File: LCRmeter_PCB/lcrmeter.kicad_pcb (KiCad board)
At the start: 2 copper layers, 71.9 x 54.1 mm, 63 parts, among them J1 LCR_input, J2 LCR_input, J3 Conn_01x06, J4 USB_B_Micro, J5 OSCILLOSCOPE, J6 misc, J7 misc, SW1 power, SW2 +, SW3 -, SW4 ok, SW5 back, U1 MCP47, U2 STM32F103C8Tx, U3 OLED, U4 74HC14, U5 MCP6001-OT, Y1 8Mhz

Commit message: added brief documentation for part of software, and license
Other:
- board text added: "COPYRIGHT(c) 2019 Rafał Mazurkiewicz"
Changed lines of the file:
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@@
   (general
     (thickness 1.6)
-    (drawings 8)
+    (drawings 9)
     (tracks 919)
     (zones 0)
@@
     )
   )
+  (gr_text "COPYRIGHT(c) 2019 Rafał Mazurkiewicz" (at 152.55 146.5) (layer B.SilkS)
+    (effects (font (size 1.5 1.5) (thickness 0.3)) (justify mirror))
+  )
   (dimension 54.102 (width 0.3) (layer Cmts.User)

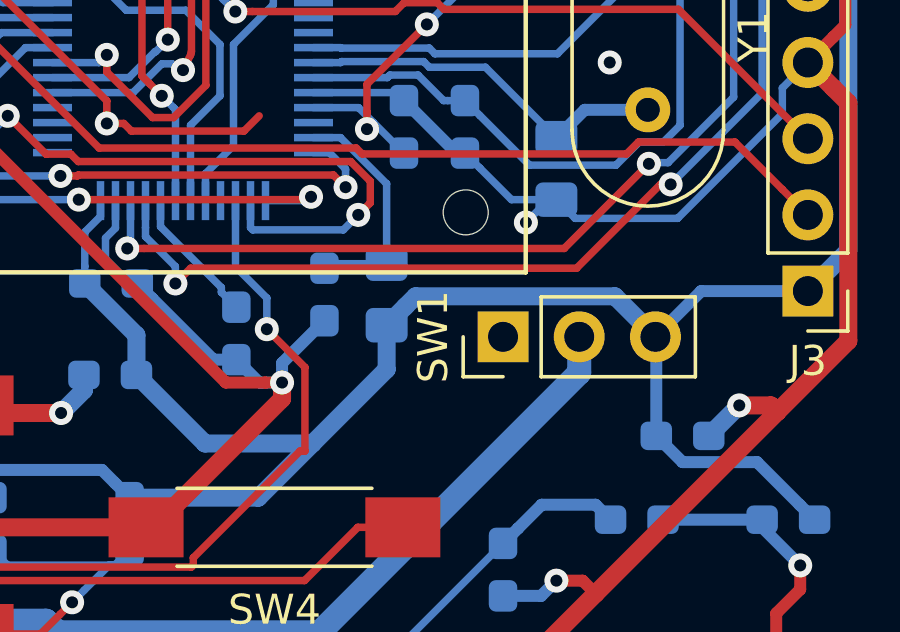
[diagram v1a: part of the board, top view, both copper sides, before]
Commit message: fixed schematic- diode reference and minor problems
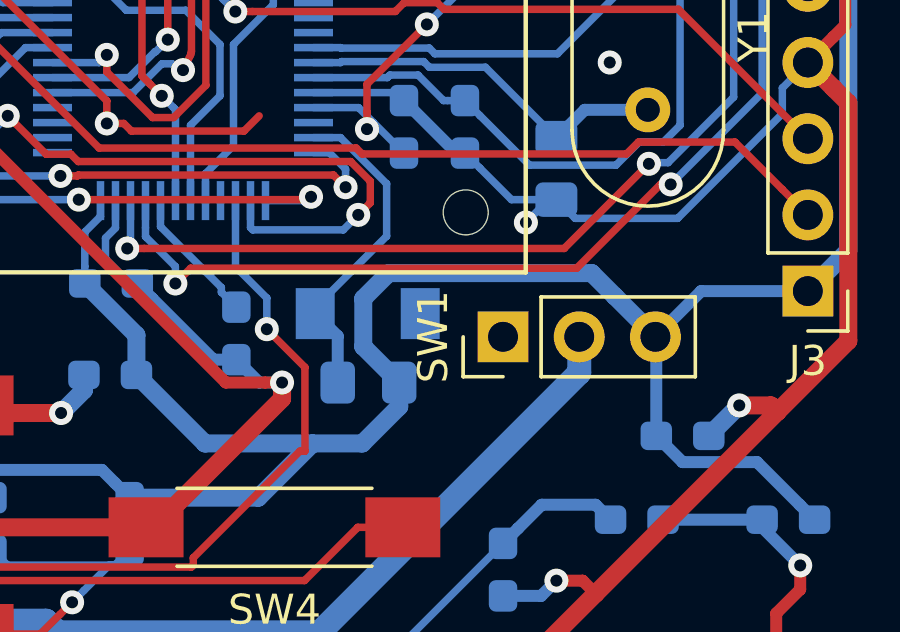
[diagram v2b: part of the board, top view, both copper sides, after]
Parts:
- removed R20: 10k, Resistor_SMD:R_0603_1608Metric_Pad1.05x0.95mm_HandSolder
- added D1: 2V, Diode_SMD:D_MiniMELF, B.Cu at (158.1, 134.1)
- J3: value Conn_01x06 -> Prog_interface
- moved R19 3.00 mm to (158.1, 136.4), turned to 180 degrees
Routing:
- net VCC: track 276.7 -> 280.3 mm
- net Net-(D1-Pad1): track 7.88 -> 11.0 mm
- net GND: track 409.3 -> 406.7 mm

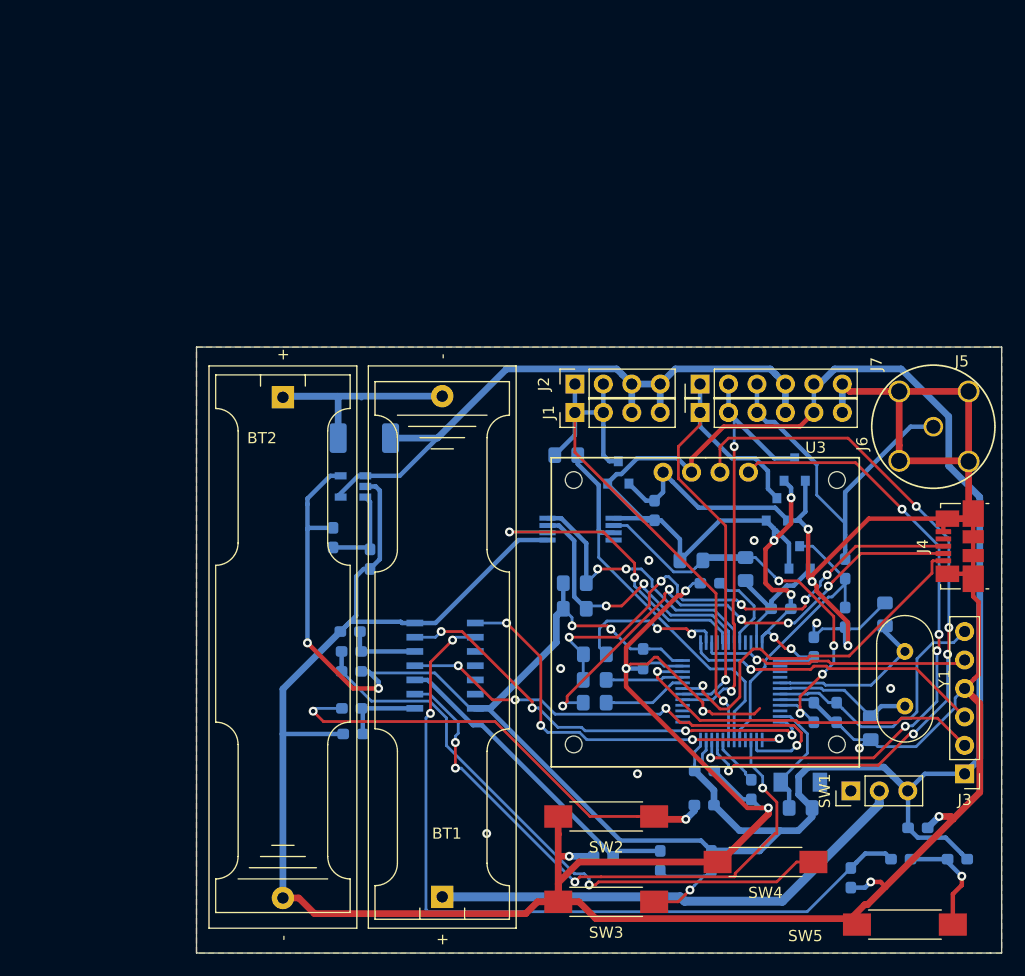
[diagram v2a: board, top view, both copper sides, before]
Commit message: placed components on PCB
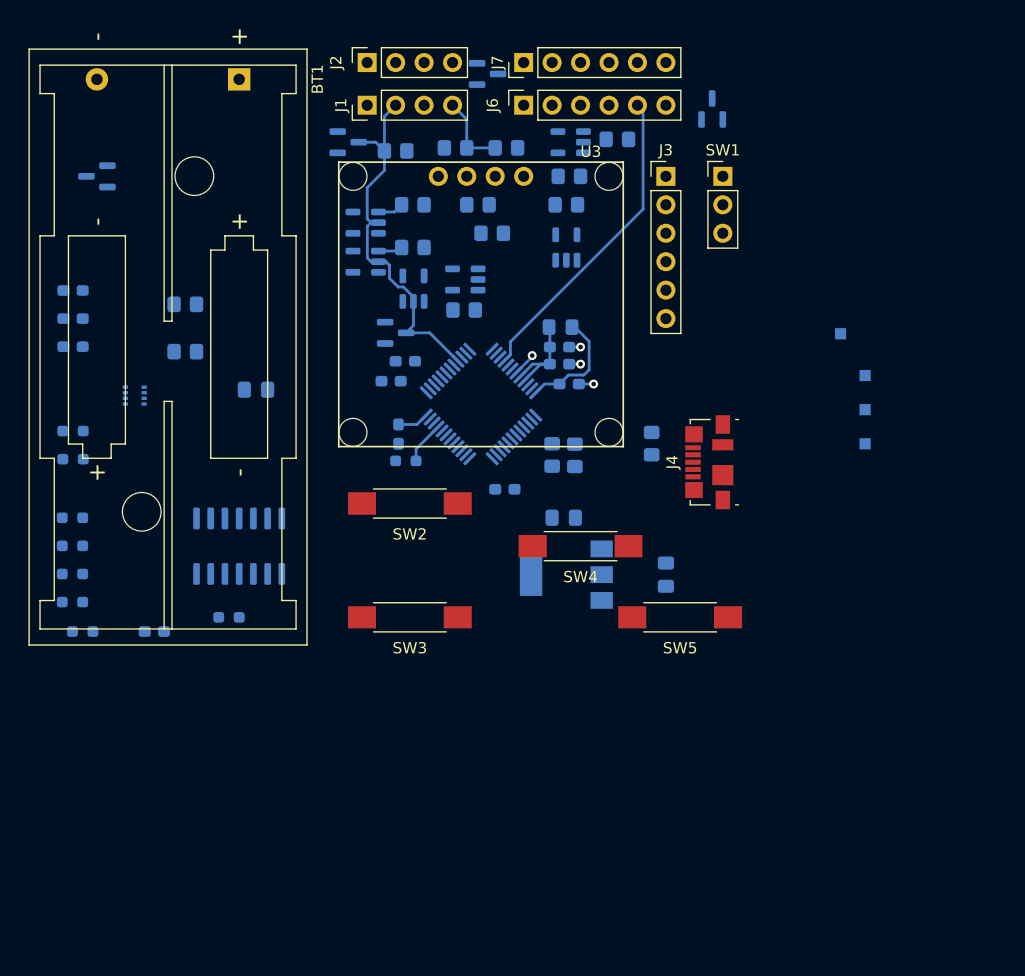
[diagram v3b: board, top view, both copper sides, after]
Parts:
- removed BT2: Batt, Battery:BatteryHolder_Keystone_2466_1xAAA
- removed C1, C2: 20pF, Capacitor_SMD:C_0805_2012Metric_Pad1.15x1.40mm_HandSolder
- removed C6: 100n, Capacitor_SMD:C_0603_1608Metric_Pad1.05x0.95mm_HandSolder
- removed D1: 2V, Diode_SMD:D_MiniMELF
- removed D5: BAT54S, Package_TO_SOT_SMD:SOT-23
- removed J5: OSCILLOSCOPE, footprints:BNC TE CONNECTIVITY 5-1634503
- removed Y1: 8Mhz, Crystal:Crystal_HC49-U_Vertical
- added C18: 10u, Capacitor_SMD:C_0805_2012Metric_Pad1.18x1.45mm_HandSolder, B.Cu at (146.1, 115.6)
- added C19: 10u, Capacitor_SMD:C_0805_2012Metric_Pad1.18x1.45mm_HandSolder, B.Cu at (136.9, 110.5)
- added D6: BAT54CW, Package_TO_SOT_SMD:SOT-23, B.Cu at (95.2, 80.0)
- added IC1: TPS2116DRLR, Library_Loader:SOTFL50P160X60-8N, B.Cu at (98.6, 99.6)
- added Q1: NX7002BKR, Package_TO_SOT_SMD:SOT-23, B.Cu at (121.9, 94.0)
- added R20: 0, Resistor_SMD:R_0805_2012Metric_Pad1.20x1.40mm_HandSolder, B.Cu at (128.0, 91.9)
- added R24: 1k5, Resistor_SMD:R_0805_2012Metric_Pad1.20x1.40mm_HandSolder, B.Cu at (103.1, 91.4)
- added R25: 2k2, Resistor_SMD:R_0805_2012Metric_Pad1.20x1.40mm_HandSolder, B.Cu at (103.1, 95.7)
- added TP1: TestPoint, TestPoint:TestPoint_Pad_1.0x1.0mm, B.Cu at (161.6, 94.1)
- added TP2: TestPoint, TestPoint:TestPoint_Pad_1.0x1.0mm, B.Cu at (163.8, 97.8)
- added TP3: TestPoint, TestPoint:TestPoint_Pad_1.0x1.0mm, B.Cu at (163.8, 100.8)
- added TP4: TestPoint, TestPoint:TestPoint_Pad_1.0x1.0mm, B.Cu at (163.8, 103.9)
- added U10: MCP6001-OT, Package_TO_SOT_SMD:SOT-23-5, B.Cu at (137.2, 86.4)
- added U6: STM32G473C_B-C-E_Tx, Package_QFP:LQFP-48_7x7mm_P0.5mm, B.Cu at (129.5, 100.3)
- added U7: 74LVC1G66, Package_TO_SOT_SMD:SOT-23-5, B.Cu at (123.5, 90.0)
- added U8: MCP6001-OT, Package_TO_SOT_SMD:SOT-23-5, B.Cu at (137.5, 77.0)
- added U9: LM1117MP-3.3, Package_TO_SOT_SMD:SOT-223-3_TabPin2, B.Cu at (137.2, 115.6)
- BT1: footprint Battery:BatteryHolder_Keystone_2466_1xAAA -> Battery:BatteryHolder_Keystone_2468_2xAAA
- C10, C12, C13, C14, C15, C3, C4, C5, C7, C9: footprint Capacitor_SMD:C_0603_1608Metric_Pad1.05x0.95mm_HandSolder -> Capacitor_SMD:C_0603_1608Metric_Pad1.08x0.95mm_HandSolder
- C11: footprint Capacitor_SMD:C_0805_2012Metric_Pad1.15x1.40mm_HandSolder -> Capacitor_SMD:C_0603_1608Metric_Pad1.08x0.95mm_HandSolder
- C8: footprint Capacitor_SMD:C_0603_1608Metric_Pad1.05x0.95mm_HandSolder -> Capacitor_SMD:C_0805_2012Metric_Pad1.18x1.45mm_HandSolder
- R1, R15: footprint Resistor_SMD:R_0805_2012Metric_Pad1.15x1.40mm_HandSolder -> Resistor_SMD:R_0805_2012Metric_Pad1.20x1.40mm_HandSolder
- R10, R11, R12, R13, R2, R4, R5, R6, R9: footprint Resistor_SMD:R_0603_1608Metric_Pad1.05x0.95mm_HandSolder -> Resistor_SMD:R_0603_1608Metric_Pad0.98x0.95mm_HandSolder
- R14, R16: value 22 -> 1k5; footprint Resistor_SMD:R_0805_2012Metric_Pad1.15x1.40mm_HandSolder -> Resistor_SMD:R_0805_2012Metric_Pad1.20x1.40mm_HandSolder
- R17, R3: value 10k -> 0; footprint Resistor_SMD:R_0603_1608Metric_Pad1.05x0.95mm_HandSolder -> Resistor_SMD:R_0805_2012Metric_Pad1.20x1.40mm_HandSolder
- R18: value 10k -> 2k; footprint Resistor_SMD:R_0603_1608Metric_Pad1.05x0.95mm_HandSolder -> Resistor_SMD:R_0805_2012Metric_Pad1.20x1.40mm_HandSolder
- R19: value 20k -> 500; footprint Resistor_SMD:R_0805_2012Metric_Pad1.15x1.40mm_HandSolder -> Resistor_SMD:R_0805_2012Metric_Pad1.20x1.40mm_HandSolder
- R21: footprint Resistor_SMD:R_2010_5025Metric_Pad1.52x2.65mm_HandSolder -> Resistor_SMD:R_0805_2012Metric_Pad1.20x1.40mm_HandSolder
- R22, R23: footprint Resistor_SMD:R_0603_1608Metric_Pad1.05x0.95mm_HandSolder -> Resistor_SMD:R_0805_2012Metric_Pad1.20x1.40mm_HandSolder
- R7, R8: value 3k3 -> 0; footprint Resistor_SMD:R_0805_2012Metric_Pad1.15x1.40mm_HandSolder -> Resistor_SMD:R_0805_2012Metric_Pad1.20x1.40mm_HandSolder
- SW2: value + -> up
- SW3: value - -> down
- U1: value MCP47 -> 74LVC1G66; footprint Package_SO:TSSOP-8_4.4x3mm_P0.65mm -> Package_TO_SOT_SMD:SOT-23-5
- U2: value STM32F103C8Tx -> 74LVC1G66; footprint Package_QFP:LQFP-48_7x7mm_P0.5mm -> Package_TO_SOT_SMD:SOT-23-5
- moved C13 87.0 mm to (93.1, 90.2), turned to 180 degrees
- moved R5 86.7 mm to (93.1, 105.3)
- moved R11 79.1 mm to (93.1, 113.0), turned to 180 degrees
- moved BT1 75.2 mm to (108.0, 71.3), turned to -90 degrees
- moved C8 70.9 mm to (109.5, 99.1), turned to 180 degrees
- moved C15 65.7 mm to (93.1, 95.2)
- moved R19 64.0 mm to (123.5, 82.5)
- moved R9 59.7 mm to (94.0, 120.7), turned to 180 degrees
- moved J3 59.6 mm to (146.1, 80.0), turned to 0 degrees
- moved R13 57.3 mm to (93.1, 118.0), turned to 180 degrees
- moved SW1 56.0 mm to (151.1, 80.0), turned to 0 degrees
- moved R17 51.2 mm to (127.3, 77.5), turned to 180 degrees
- moved R18 50.8 mm to (123.5, 86.4), turned to 180 degrees
- moved U2 50.4 mm to (119.2, 87.6)
- moved C10 49.7 mm to (122.8, 96.5), turned to 0 degrees
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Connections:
- BT1 pad 2: Net-(BT1-Pad2) -> GND
- D3 pad 3: /OSCILLOSCOPE -> /OSCILLOSCOPE_IN
- J1 pad 3: +1V5 -> Net-(J1-Pin_3)
- J1 pad 4: +1V5 -> Net-(J1-Pin_3)
- J2 pad 3: +1V5 -> Net-(J1-Pin_3)
- J2 pad 4: +1V5 -> Net-(J1-Pin_3)
- J3 pad 2: Net-(J3-Pad2) -> Net-(J3-Pin_2)
- J3 pad 3: Net-(J3-Pad3) -> Net-(J3-Pin_3)
- J4 pad 1: /VBUS -> VBUS
- J4 pad 2: Net-(J4-Pad2) -> /USB_-
- J4 pad 3: Net-(J4-Pad3) -> /USB_+
- J4 pad 4: Net-(J4-Pad4) -> unconnected-(J4-ID-Pad4)
- J4 pad 6: GND -> unconnected-(J4-Shield-Pad6)
- J6 pad 1: /PWM_OUT -> VCC
- J6 pad 2: /8_MHz_OUT -> /PWM_OUT
- J6 pad 3: /OSCILLOSCOPE_IN -> /WAVE_OUT
- J6 pad 4: +1V5 -> GND
- J6 pad 5: VCC -> /OSCILLOSCOPE_IN
- J7 pad 1: /PWM_OUT -> VCC
- J7 pad 2: /8_MHz_OUT -> /PWM_OUT
- J7 pad 3: /OSCILLOSCOPE_IN -> /WAVE_OUT
- J7 pad 4: +1V5 -> GND
- J7 pad 5: VCC -> /OSCILLOSCOPE_IN
- R14 pad 1: Net-(J4-Pad2) -> VCC
- R14 pad 2: /USB_- -> /SDA
- R15 pad 2: Net-(J4-Pad3) -> /USB_+
- R16 pad 1: Net-(J4-Pad3) -> VCC
- R16 pad 2: /USB_+ -> /SCL
- R17 pad 1: /OSCILLOSCOPE_IN -> Net-(J1-Pin_3)
- R17 pad 2: /OSCILLOSCOPE -> GND
- R18 pad 1: /OSCILLOSCOPE -> /ADC_1
- R18 pad 2: GND -> Net-(R18-Pad2)
- R19 pad 1: VCC -> /ADC_1
- R19 pad 2: Net-(D1-Pad1) -> Net-(R19-Pad2)
- R2 pad 2: Net-(R2-Pad2) -> Net-(U6-PB8)
- R21 pad 1: +1V5 -> Net-(U8-+)
- R21 pad 2: Net-(BT1-Pad2) -> +1V5
- R22 pad 1: VCC -> Net-(U8-+)
- R22 pad 2: Net-(R22-Pad2) -> VCC
- R23 pad 1: Net-(R22-Pad2) -> GND
- R23 pad 2: GND -> Net-(U8-+)
- R3 pad 1: GND -> /ADC_1
- R3 pad 2: Net-(R3-Pad2) -> /ADC_1b
- R7 pad 1: VCC -> /ADC_2
- R7 pad 2: /I2C_SCL -> /ADC_2b
- R8 pad 1: VCC -> Net-(J1-Pin_3)
- R8 pad 2: /I2C_SDA -> +1V5
- SW1 pad 1: Net-(SW1-Pad1) -> unconnected-(SW1-Pad1)
- SW1 pad 3: VCC -> +BATT
- U1 pad 1: VCC -> Net-(R19-Pad2)
- U1 pad 2: VDDA -> /ADC_2
- U1 pad 3: /ADC_1 -> GND
- U1 pad 4: Net-(U1-Pad4) -> /EN_PATH_1
- U1 pad 5: GND -> VCC
- U2 pad 1: VCC -> Net-(R18-Pad2)
- U2 pad 2: Net-(U2-Pad2) -> /ADC_2
- U2 pad 3: Net-(U2-Pad3) -> GND
- U2 pad 4: Net-(U2-Pad4) -> /EN_PATH_2
- U2 pad 5: Net-(C2-Pad1) -> VCC
- U3 pad 1: Net-(U2-Pad22) -> /SDA
- U3 pad 2: Net-(U2-Pad21) -> /SCL
- U5 pad 1: +1V5 -> /ADC_1
- U5 pad 3: Net-(R22-Pad2) -> /DAC_UNBUFFERED
- U5 pad 4: +1V5 -> /ADC_1
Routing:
- net GND: track 406.7 -> 5.51 mm, vias 18 -> 4
- net VCC: track 280.3 -> 13.0 mm, vias 9 -> 0
- net Net-(C13-Pad1): track 71.1 -> 0.00 mm, vias 2 -> 0
- net +1V5: track 67.0 -> 0.00 mm
- net Net-(U2-Pad21): track 66.5 -> 0.00 mm, vias 5 -> 0
- net Net-(U2-Pad22): track 58.3 -> 0.00 mm, vias 5 -> 0
- net Net-(R10-Pad2): track 54.4 -> 0.00 mm, vias 1 -> 0
- net /BUTTON_+: track 53.2 -> 0.00 mm, vias 4 -> 0
- net Net-(J4-Pad3): track 45.2 -> 0.00 mm, vias 5 -> 0
- net /PWM_OUT: track 45.0 -> 0.00 mm, vias 1 -> 0
- net Net-(J4-Pad2): track 45.0 -> 0.00 mm, vias 5 -> 0
- net Net-(BT1-+): track 44.0 -> 0.00 mm
- net /BUTTON_-: track 43.4 -> 0.00 mm, vias 4 -> 0
- net Net-(R12-Pad2): track 41.5 -> 0.00 mm, vias 2 -> 0
- net /8_MHz_OUT: track 40.2 -> 0.00 mm, vias 2 -> 0
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- removed copper zone on B.Cu, net GND
- removed copper zone on F.Cu, net GND
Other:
- board outline removed
- net class Default removed
- board text removed: "COPYRIGHT(c) 2019 Rafał Mazurkiewicz"

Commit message: routing mostly done
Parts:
- removed TP1, TP2: TestPoint, TestPoint:TestPoint_Pad_1.0x1.0mm
- moved D6 52.6 mm to (129.8, 119.6), turned to -90 degrees
- moved TP3 45.2 mm to (118.9, 96.5)
- moved TP4 41.5 mm to (123.4, 113.5)
- moved R24 34.7 mm to (128.5, 115.0), turned to -90 degrees
- moved R25 33.6 mm to (130.6, 115.0), turned to 90 degrees
- moved IC1 31.2 mm to (125.7, 115.1)
- moved R9 30.3 mm to (112.6, 96.8)
- moved R12 28.8 mm to (108.9, 91.4), turned to 0 degrees
- moved R6 28.4 mm to (112.4, 91.4)
- moved R13 26.6 mm to (109.1, 96.8), turned to 0 degrees
- moved C8 24.7 mm to (130.8, 111.5), turned to 0 degrees
- moved C12 23.3 mm to (109.1, 99.1), turned to 0 degrees
- moved R4 19.6 mm to (112.6, 100.6)
- moved R10 18.9 mm to (109.1, 100.6), turned to 0 degrees
- moved U4 17.4 mm to (102.4, 96.5), turned to 180 degrees
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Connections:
- D6 pad 2: VBUS -> /V_USB
- IC1 pad 3: VBUS -> /V_USB
- R25 pad 2: VBUS -> /V_USB
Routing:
- net VCC: track 13.0 -> 271.5 mm, vias 0 -> 3
- net GND: track 5.51 -> 98.8 mm, vias 4 -> 46
- net Net-(R11-Pad2): track 0.00 -> 72.0 mm, vias 0 -> 1
- net Net-(BT1-+): track 0.00 -> 69.0 mm
- net /PWM_OUT: track 0.00 -> 62.8 mm, vias 0 -> 1
- net Net-(J3-Pin_2): track 0.00 -> 56.9 mm, vias 0 -> 2
- net Net-(J3-Pin_3): track 0.00 -> 52.2 mm, vias 0 -> 2
- net +BATT: track 0.00 -> 51.9 mm
- net /SWO: track 0.00 -> 51.1 mm, vias 0 -> 2
- net +1V5: track 0.00 -> 50.0 mm, vias 0 -> 2
- net /V_USB: track 0.00 -> 46.8 mm, vias 0 -> 2
- net Net-(R10-Pad2): track 0.00 -> 42.6 mm, vias 0 -> 1
- net /ADC_1: track 0.00 -> 42.3 mm, vias 0 -> 2
- net /BUTTON_+: track 0.00 -> 36.1 mm, vias 0 -> 2
- net /SCL: track 0.00 -> 35.0 mm, vias 0 -> 1
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- added copper zone on B.Cu, net GND
- added copper zone on F.Cu, net GND
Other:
- board outline added: 64 x 55.2 mm

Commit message: PCB done, needs review
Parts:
- moved D3 3.92 mm to (146.7, 76.8), turned to 180 degrees
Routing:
- net GND: track 98.8 -> 118.6 mm, vias 46 -> 48
- net /OSCILLOSCOPE_IN: track 39.2 -> 33.7 mm
- net VCC: track 271.5 -> 269.2 mm
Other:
- board text added: "LCRmeter v3 2023 Rafał Mazurkiewicz"
